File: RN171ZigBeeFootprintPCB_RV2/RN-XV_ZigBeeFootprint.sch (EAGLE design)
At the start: 20 parts

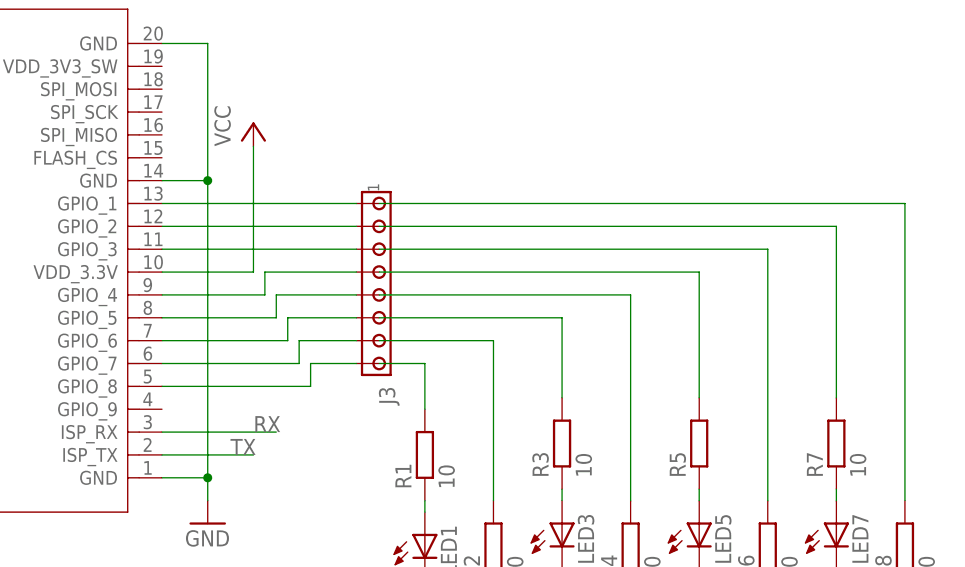
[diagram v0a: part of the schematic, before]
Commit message: Wired LED in to the PCB design.
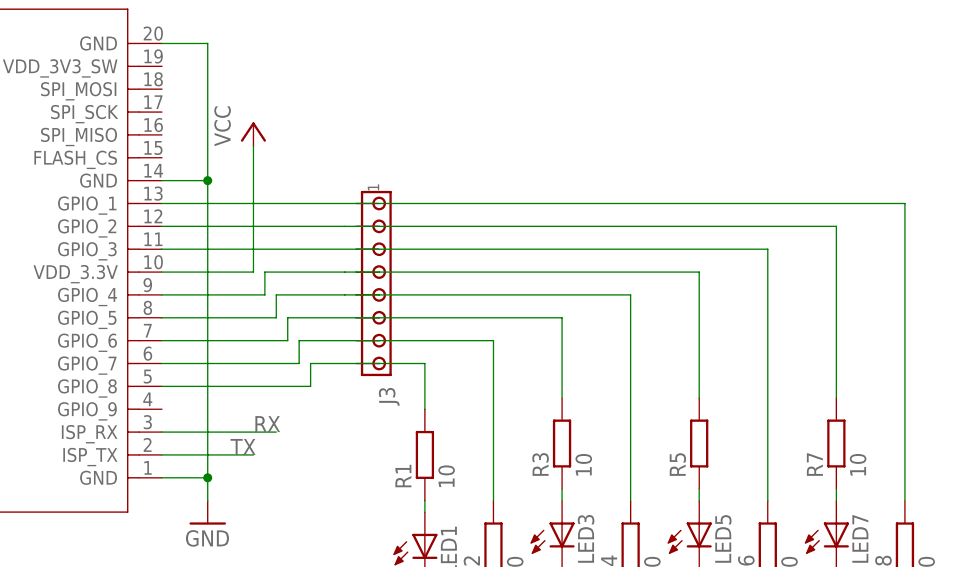
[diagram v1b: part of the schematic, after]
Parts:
- LED1, LED2, LED3, LED4, LED5, LED6, LED7, LED8: device eagle-ltspice:LED_ESML0603 -> eagle-ltspice:LED_ELD260
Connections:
- removed net N$12: J1.GPIO_1, J3.1
- removed net N$13: J1.GPIO_2, J3.2
- removed net N$14: J1.GPIO_3, J3.3
- removed net N$15: J1.GPIO_4, J3.4
- removed net N$16: J1.GPIO_5, J3.5
- removed net N$17: J1.GPIO_6, J3.6
- removed net N$18: J1.GPIO_7, J3.7
- removed net N$19: J1.GPIO_8, J3.8
- net N$30: now also J1.GPIO_8, J3.8
- net N$31: now also J1.GPIO_7, J3.7
- net N$32: now also J1.GPIO_6, J3.6
- net N$33: now also J1.GPIO_5, J3.5
- net N$34: now also J1.GPIO_4, J3.4
- net N$35: now also J1.GPIO_3, J3.3
- net N$36: now also J1.GPIO_2, J3.2
- net N$37: now also J1.GPIO_1, J3.1

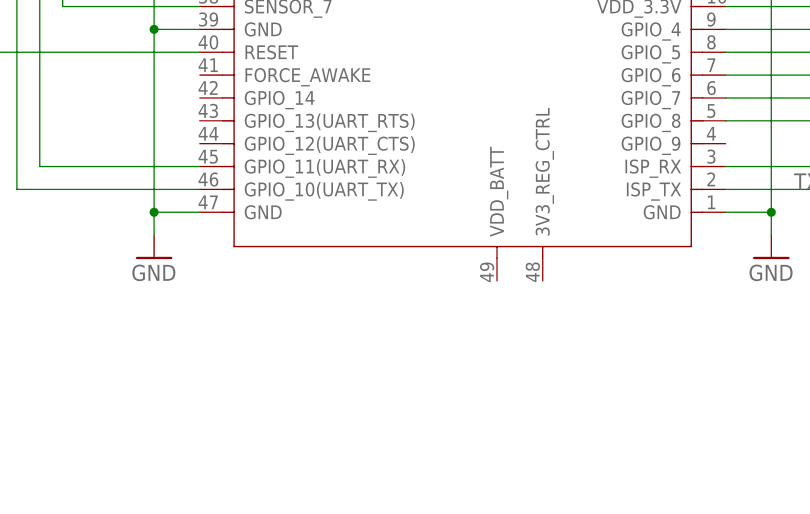
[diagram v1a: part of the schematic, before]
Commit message: Connecting voltage supply to all components.
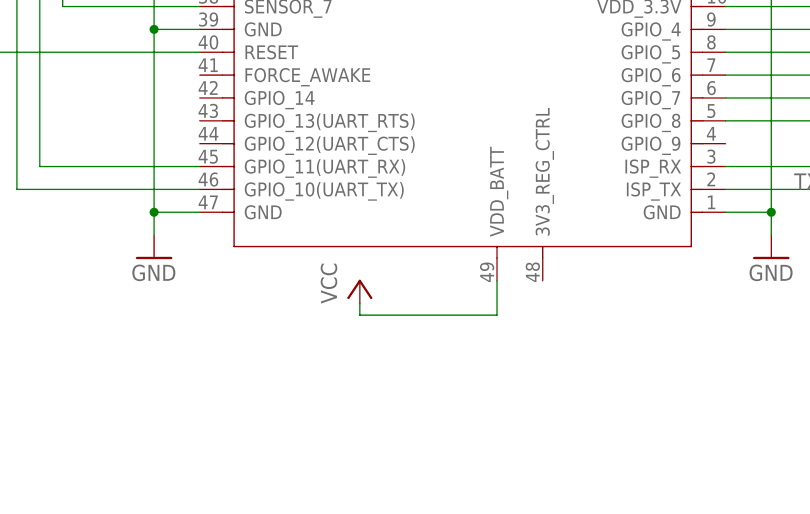
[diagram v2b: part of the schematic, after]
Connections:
- removed net VCC: XB1.VCC
- net VDD_3.3V: now also J1.VDD_BATT, XB1.VCC
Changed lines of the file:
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@@
 <grid distance="0.05" unitdist="inch" unit="inch" style="lines" multiple="1" display="no" altdistance="0.01" altunitdist="inch" altunit="inch"/>
 <layers>
-<layer number="1" name="Top" color="4" fill="1" visible="yes" active="no"/>
-<layer number="2" name="Route2" color="1" fill="3" visible="yes" active="no"/>
-<layer number="3" name="Route3" color="4" fill="3" visible="yes" active="no"/>
-<layer number="4" name="Route4" color="1" fill="4" visible="yes" active="no"/>
-<layer number="5" name="Route5" color="4" fill="4" visible="yes" active="no"/>
-<layer number="6" name="Route6" color="1" fill="8" visible="yes" active="no"/>
-<layer number="7" name="Route7" color="4" fill="8" visible="yes" active="no"/>
-<layer number="8" name="Route8" color="1" fill="2" visible="yes" active="no"/>
-<layer number="9" name="Route9" color="4" fill="2" visible="yes" active="no"/>
-<layer number="10" name="Route10" color="1" fill="7" visible="yes" active="no"/>
-<layer number="11" name="Route11" color="4" fill="7" visible="yes" active="no"/>
-<layer number="12" name="Route12" color="1" fill="5" visible="yes" active="no"/>
-<layer number="13" name="Route13" color="4" fill="5" visible="yes" active="no"/>
-<layer number="14" name="Route14" color="1" fill="6" visible="yes" active="no"/>
-<layer number="15" name="Route15" color="4" fill="6" visible="yes" active="no"/>
-<layer number="16" name="Bottom" color="1" fill="1" visible="yes" active="no"/>
-<layer number="17" name="Pads" color="2" fill="1" visible="yes" active="no"/>
-<layer number="18" name="Vias" color="2" fill="1" visible="yes" active="no"/>
-<layer number="19" name="Unrouted" color="6" fill="1" visible="yes" active="no"/>
-<layer number="20" name="Dimension" color="15" fill="1" visible="yes" active="no"/>
-<layer number="21" name="tPlace" color="7" fill="1" visible="yes" active="no"/>
-<layer number="22" name="bPlace" color="7" fill="1" visible="yes" active="no"/>
-<layer number="23" name="tOrigins" color="15" fill="1" visible="yes" active="no"/>
-<layer number="24" name="bOrigins" color="15" fill="1" visible="yes" active="no"/>
-<layer number="25" name="tNames" color="7" fill="1" visible="yes" active="no"/>
-<layer number="26" name="bNames" color="7" fill="1" visible="yes" active="no"/>
-<layer number="27" name="tValues" color="7" fill="1" visible="yes" active="no"/>
-<layer number="28" name="bValues" color="7" fill="1" visible="yes" active="no"/>
+<layer number="1" name="Top" color="4" fill="1" visible="no" active="no"/>
+<layer number="2" name="Route2" color="1" fill="3" visible="no" active="no"/>
+<layer number="3" name="Route3" color="4" fill="3" visible="no" active="no"/>
+<layer number="4" name="Route4" color="1" fill="4" visible="no" active="no"/>
+<layer number="5" name="Route5" color="4" fill="4" visible="no" active="no"/>
+<layer number="6" name="Route6" color="1" fill="8" visible="no" active="no"/>
+<layer number="7" name="Route7" color="4" fill="8" visible="no" active="no"/>
+<layer number="8" name="Route8" color="1" fill="2" visible="no" active="no"/>
+<layer number="9" name="Route9" color="4" fill="2" visible="no" active="no"/>
+<layer number="10" name="Route10" color="1" fill="7" visible="no" active="no"/>
+<layer number="11" name="Route11" color="4" fill="7" visible="no" active="no"/>
+<layer number="12" name="Route12" color="1" fill="5" visible="no" active="no"/>
+<layer number="13" name="Route13" color="4" fill="5" visible="no" active="no"/>
+<layer number="14" name="Route14" color="1" fill="6" visible="no" active="no"/>
+<layer number="15" name="Route15" color="4" fill="6" visible="no" active="no"/>
+<layer number="16" name="Bottom" color="1" fill="1" visible="no" active="no"/>
+<layer number="17" name="Pads" color="2" fill="1" visible="no" active="no"/>
+<layer number="18" name="Vias" color="2" fill="1" visible="no" active="no"/>
+<layer number="19" name="Unrouted" color="6" fill="1" visible="no" active="no"/>
+<layer number="20" name="Dimension" color="15" fill="1" visible="no" active="no"/>
+<layer number="21" name="tPlace" color="7" fill="1" visible="no" active="no"/>
+<layer number="22" name="bPlace" color="7" fill="1" visible="no" active="no"/>
+<layer number="23" name="tOrigins" color="15" fill="1" visible="no" active="no"/>
+<layer number="24" name="bOrigins" color="15" fill="1" visible="no" active="no"/>
+<layer number="25" name="tNames" color="7" fill="1" visible="no" active="no"/>
+<layer number="26" name="bNames" color="7" fill="1" visible="no" active="no"/>
+<layer number="27" name="tValues" color="7" fill="1" visible="no" active="no"/>
+<layer number="28" name="bValues" color="7" fill="1" visible="no" active="no"/>
 <layer number="29" name="tStop" color="7" fill="3" visible="no" active="no"/>
 <layer number="30" name="bStop" color="7" fill="6" visible="no" active="no"/>
@@
 <layer number="35" name="tGlue" color="7" fill="4" visible="no" active="no"/>
 <layer number="36" name="bGlue" color="7" fill="5" visible="no" active="no"/>
-<layer number="37" name="tTest" color="7" fill="1" visible="yes" active="no"/>
-<layer number="38" name="bTest" color="7" fill="1" visible="yes" active="no"/>
+<layer number="37" name="tTest" color="7" fill="1" visible="no" active="no"/>
+<layer number="38" name="bTest" color="7" fill="1" visible="no" active="no"/>
 <layer number="39" name="tKeepout" color="4" fill="11" visible="no" active="no"/>
 <layer number="40" name="bKeepout" color="1" fill="11" visible="no" active="no"/>
@@
 <layer number="44" name="Drills" color="7" fill="1" visible="no" active="no"/>
 <layer number="45" name="Holes" color="7" fill="1" visible="no" active="no"/>
-<layer number="46" name="Milling" color="3" fill="1" visible="yes" active="no"/>
-<layer number="47" name="Measures" color="7" fill="1" visible="yes" active="no"/>
-<layer number="48" name="Document" color="7" fill="1" visible="yes" active="no"/>
-<layer number="49" name="Reference" color="7" fill="1" visible="yes" active="no"/>
-<layer number="50" name="dxf" color="7" fill="1" visible="yes" active="no"/>
-<layer number="51" name="tDocu" color="7" fill="1" visible="yes" active="no"/>
-<layer number="52" name="bDocu" color="7" fill="1" visible="yes" active="no"/>
-<layer number="53" name="tGND_GNDA" color="7" fill="9" visible="yes" active="no"/>
-<layer number="54" name="bGND_GNDA" color="1" fill="9" visible="yes" active="no"/>
-<layer number="56" name="wert" color="7" fill="1" visible="yes" active="no"/>
+<layer number="46" name="Milling" color="3" fill="1" visible="no" active="no"/>
+<layer number="47" name="Measures" color="7" fill="1" visible="no" active="no"/>
+<layer number="48" name="Document" color="7" fill="1" visible="no" active="no"/>
+<layer number="49" name="Reference" color="7" fill="1" visible="no" active="no"/>
+<layer number="50" name="dxf" color="7" fill="1" visible="no" active="no"/>
+<layer number="51" name="tDocu" color="7" fill="1" visible="no" active="no"/>
+<layer number="52" name="bDocu" color="7" fill="1" visible="no" active="no"/>
+<layer number="53" name="tGND_GNDA" color="7" fill="9" visible="no" active="no"/>
+<layer number="54" name="bGND_GNDA" color="1" fill="9" visible="no" active="no"/>
+<layer number="56" name="wert" color="7" fill="1" visible="no" active="no"/>
 <layer number="91" name="Nets" color="2" fill="1" visible="yes" active="yes"/>
 <layer number="92" name="Busses" color="1" fill="1" visible="yes" active="yes"/>
@@
 <part name="LED8" library="eagle-ltspice" deviceset="LED_E" device="LD260"/>
 <part name="GND4" library="supply1" deviceset="GND" device=""/>
+<part name="P+3" library="supply1" deviceset="VCC" device=""/>
 </parts>
 <sheets>
@@
 <instance part="LED8" gate="G$1" x="238.76" y="59.69"/>
 <instance part="GND4" gate="1" x="238.76" y="48.26"/>
+<instance part="P+3" gate="VCC" x="115.57" y="68.58"/>
 </instances>
 <busses>
@@
 </segment>
 </net>
-<net name="VCC" class="0">
+<net name="VDD_3.3V" class="0">
+<segment>
+<pinref part="P+2" gate="VCC" pin="VCC"/>
+<wire x1="166.37" y1="113.03" x2="166.37" y2="99.06" width="0.1524" layer="91"/>
+<wire x1="166.37" y1="99.06" x2="156.21" y2="99.06" width="0.1524" layer="91"/>
+<pinref part="J1" gate="G$1" pin="VDD_3.3V"/>
+</segment>
+<segment>
+<pinref part="J1" gate="G$1" pin="VDD_BATT"/>
+<wire x1="130.81" y1="68.58" x2="130.81" y2="64.77" width="0.1524" layer="91"/>
+<pinref part="P+3" gate="VCC" pin="VCC"/>
+<wire x1="130.81" y1="64.77" x2="115.57" y2="64.77" width="0.1524" layer="91"/>
+<wire x1="115.57" y1="64.77" x2="115.57" y2="66.04" width="0.1524" layer="91"/>
+</segment>
 <segment>
 <pinref part="XB1" gate="G$1" pin="VCC"/>
@@
 </segment>
 </net>
-<net name="VDD_3.3V" class="0">
-<segment>
-<pinref part="P+2" gate="VCC" pin="VCC"/>
-<wire x1="166.37" y1="113.03" x2="166.37" y2="99.06" width="0.1524" layer="91"/>
-<wire x1="166.37" y1="99.06" x2="156.21" y2="99.06" width="0.1524" layer="91"/>
-<pinref part="J1" gate="G$1" pin="VDD_3.3V"/>
-</segment>
-</net>

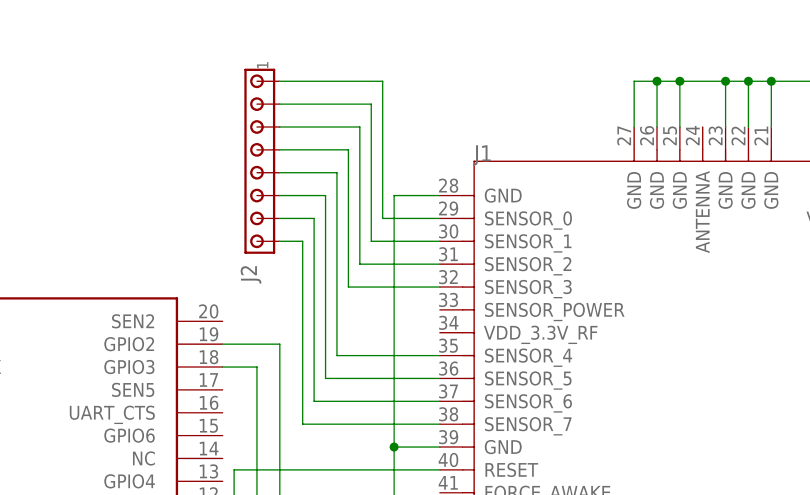
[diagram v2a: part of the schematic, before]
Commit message: Connecting RN171's 34 pin to VCC
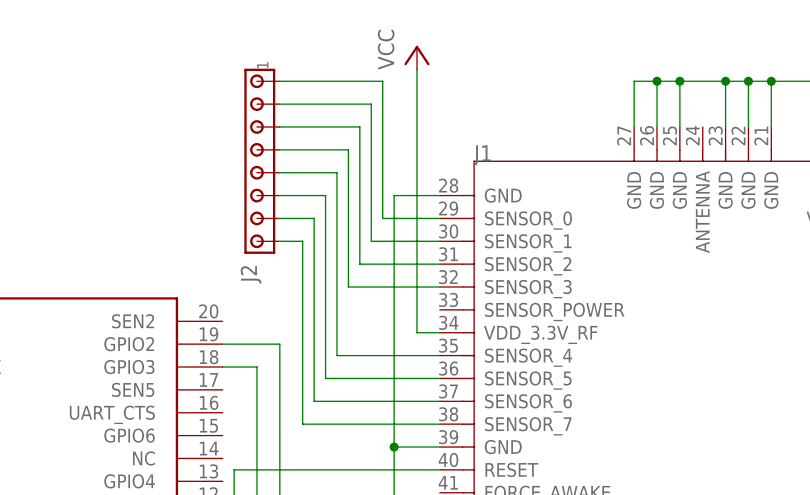
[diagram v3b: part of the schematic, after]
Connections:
- net VDD_3.3V: now also J1.VDD_3.3V_RF
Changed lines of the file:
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@@
 <part name="GND4" library="supply1" deviceset="GND" device=""/>
 <part name="P+3" library="supply1" deviceset="VCC" device=""/>
+<part name="P+4" library="supply1" deviceset="VCC" device=""/>
 </parts>
 <sheets>
@@
 <instance part="GND4" gate="1" x="238.76" y="48.26"/>
 <instance part="P+3" gate="VCC" x="115.57" y="68.58"/>
+<instance part="P+4" gate="VCC" x="95.25" y="140.97"/>
 </instances>
 <busses>
@@
 <wire x1="31.75" y1="110.49" x2="31.75" y2="116.84" width="0.1524" layer="91"/>
 </segment>
-</net>
+<segment>
+<pinref part="P+4" gate="VCC" pin="VCC"/>
+<wire x1="95.25" y1="138.43" x2="95.25" y2="109.22" width="0.1524" layer="91"/>
+<pinref part="J1" gate="G$1" pin="VDD_3.3V_RF"/>
+<wire x1="95.25" y1="109.22" x2="97.79" y2="109.22" width="0.1524" layer="91"/>
+</segment>
+</net>
